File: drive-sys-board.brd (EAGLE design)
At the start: 109.2 x 48.3 mm, 28 parts

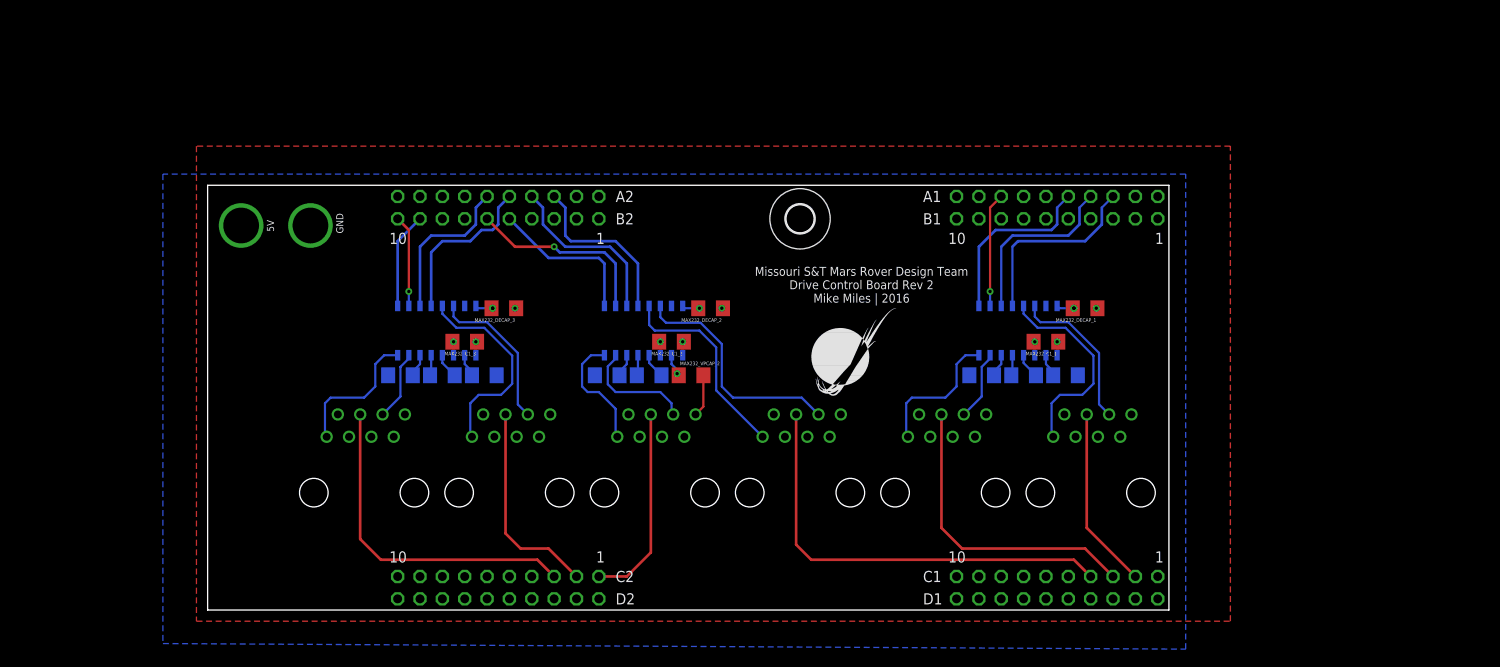
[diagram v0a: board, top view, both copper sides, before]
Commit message: Replaced RJ45 Connectors with 15-Pin D-Subs
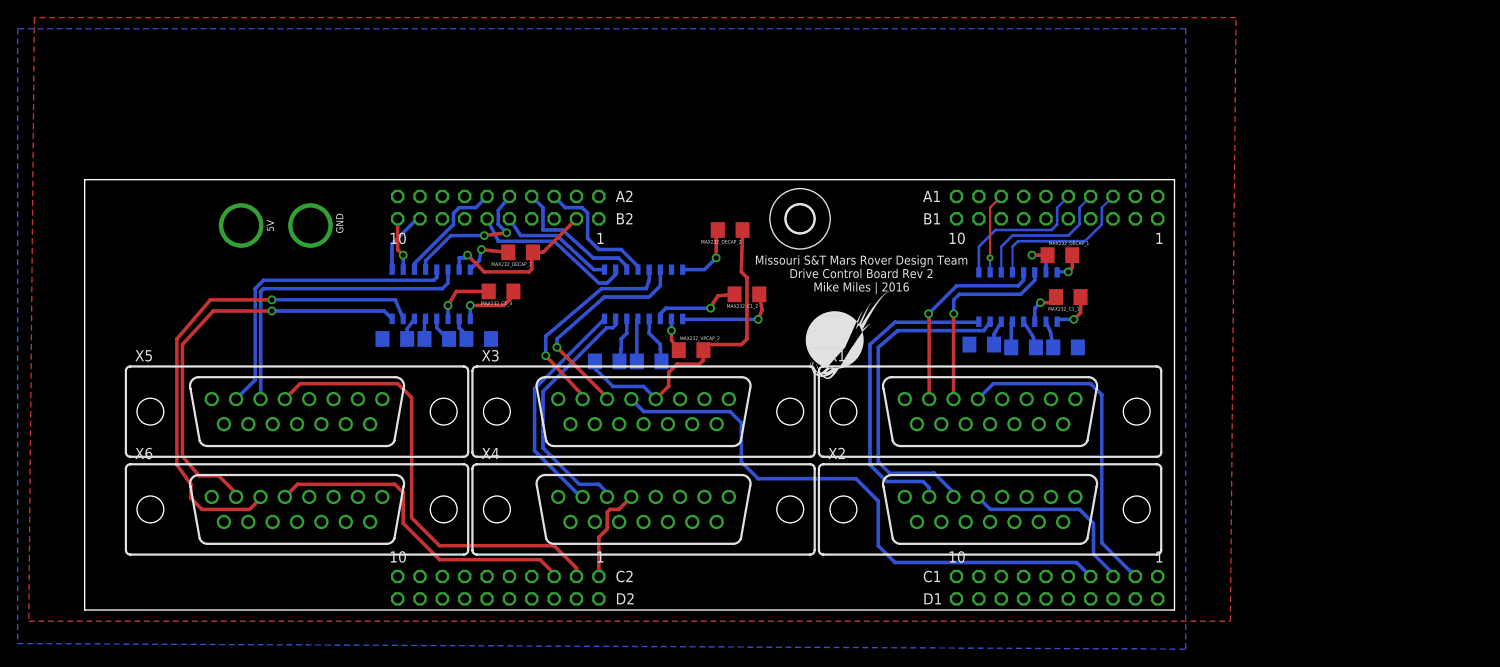
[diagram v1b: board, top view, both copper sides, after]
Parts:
- removed RJ45_1, RJ45_2, RJ45_3, RJ45_4, RJ45_5, RJ45_6: RJ45KEYSTONE-949, MRDT-2015-General:KEYSTONE-949
- added X1, X2, X3, X4, X5, X6: D-SUB15-H2M15ST, con-thomas-betts:H2M15ST
- moved MAX232_C1_2 10.1 mm to (61.3, 35.9)
- moved MAX232_DECAP_2 9.16 mm to (59.4, 43.2)
- moved MAX232_C1_3 7.05 mm to (33.3, 36.2)
- moved MAX232_DECAP_1 6.68 mm to (96.8, 40.3), turned to 0 degrees
- moved MAX232_DECAP_3 6.63 mm to (35.6, 40.6)
- moved MAX232_C1_1 5.68 mm to (97.8, 35.6)
- moved MAX232_3 4.18 mm to (25.4, 35.9)
- moved MAX232_C2_3 4.18 mm to (26.0, 30.8)
- moved MAX232_VPCAP_3 4.18 mm to (30.8, 30.8)
- moved MAX232_VNCAP_3 4.18 mm to (21.3, 30.8)
- moved MAX232_2 4.13 mm to (49.5, 35.9)
- moved MAX232_1 3.81 mm to (92.1, 35.6)
- moved MAX232_VNCAP_1 3.49 mm to (87.9, 30.2)
- moved MAX232_C2_1 3.17 mm to (92.7, 29.8)
- moved MAX232_VPCAP_1 3.17 mm to (97.5, 29.8)
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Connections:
- removed net RS232_IN_4: MAX232_2.8, RJ45_4.P$1
- new net RS232_IN__4: MAX232_2.8, X4.2
- net +5V: no longer RJ45_1.P$5, RJ45_2.P$5, RJ45_3.P$5, RJ45_4.P$5, RJ45_5.P$5, RJ45_6.P$5
- net GND: now also MAX232_2.15, MAX232_3.15, X1.13, X1.5, X2.13, X2.5, X3.13, X3.5, X4.13, X4.5, X5.13, X5.5, X6.13, X6.5; no longer RJ45_1.P$2, RJ45_1.P$3, RJ45_1.P$7, RJ45_1.P$8, RJ45_2.P$2, RJ45_2.P$3, RJ45_2.P$7, RJ45_2.P$8, RJ45_3.P$2, RJ45_3.P$3, RJ45_3.P$7, RJ45_3.P$8, RJ45_4.P$2, RJ45_4.P$3, RJ45_4.P$7, RJ45_4.P$8, RJ45_5.P$2, RJ45_5.P$3, RJ45_5.P$7, RJ45_5.P$8, RJ45_6.P$2, RJ45_6.P$3, RJ45_6.P$7, RJ45_6.P$8
- net PWM_1: now also X1.4; no longer RJ45_1.P$4
- net PWM_2: now also X2.4; no longer RJ45_2.P$4
- net PWM_3: now also X3.4; no longer RJ45_3.P$4
- net PWM_4: now also X4.4; no longer RJ45_4.P$4
- net PWM_5: now also X5.4; no longer RJ45_5.P$4
- net PWM_6: now also X6.4; no longer RJ45_6.P$4
- net RS232_IN_1: now also X1.2; no longer RJ45_1.P$1
- net RS232_IN_2: now also X2.2; no longer RJ45_2.P$1
- net RS232_IN_3: now also X3.2; no longer RJ45_3.P$1
- net RS232_IN_5: now also X5.2; no longer RJ45_5.P$1
- net RS232_IN_6: now also X6.2; no longer RJ45_6.P$1
- net RS232_OUT_1: now also X1.3; no longer RJ45_1.P$6
- net RS232_OUT_2: now also X2.3; no longer RJ45_2.P$6
- net RS232_OUT_3: now also X3.3; no longer RJ45_3.P$6
- net RS232_OUT_4: now also X4.3; no longer RJ45_4.P$6
- net RS232_OUT_5: now also X5.3; no longer RJ45_5.P$6
- net RS232_OUT_6: now also X6.3; no longer RJ45_6.P$6
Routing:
- net GND: track 4.81 -> 61.3 mm, vias 3 -> 2
- net RS232_OUT_6: track 7.96 -> 56.9 mm, vias 0 -> 1
- net RS232_IN_6: track 15.9 -> 46.9 mm, vias 0 -> 1
- net RS232_OUT_2: track 7.96 -> 37.4 mm
- net PWM_5: track 23.6 -> 51.5 mm
- net RS232_IN__4: track 0.00 -> 25.9 mm
- net RS232_IN_2: track 15.9 -> 35.9 mm
- net RS232_OUT_5: track 17.7 -> 35.4 mm
- net PWM_1: track 20.7 -> 37.6 mm
- net PWM_3: track 49.8 -> 66.1 mm
- net RS232_OUT_4: track 13.1 -> 28.4 mm
- net RS232_IN_4: track 13.6 -> 0.00 mm
- net PWM_2: track 34.7 -> 21.3 mm
- net RS232_IN_5: track 23.6 -> 35.5 mm
- net PWM_4: track 22.7 -> 11.2 mm
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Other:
- board size 109.2 x 48.3 mm -> 123.8 x 48.9 mm

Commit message: Updated connectors and UART hardware
- Replaced DSubs with Molex-SL 5-pin Connectors
- Swapped MAX3232 for MAX3078
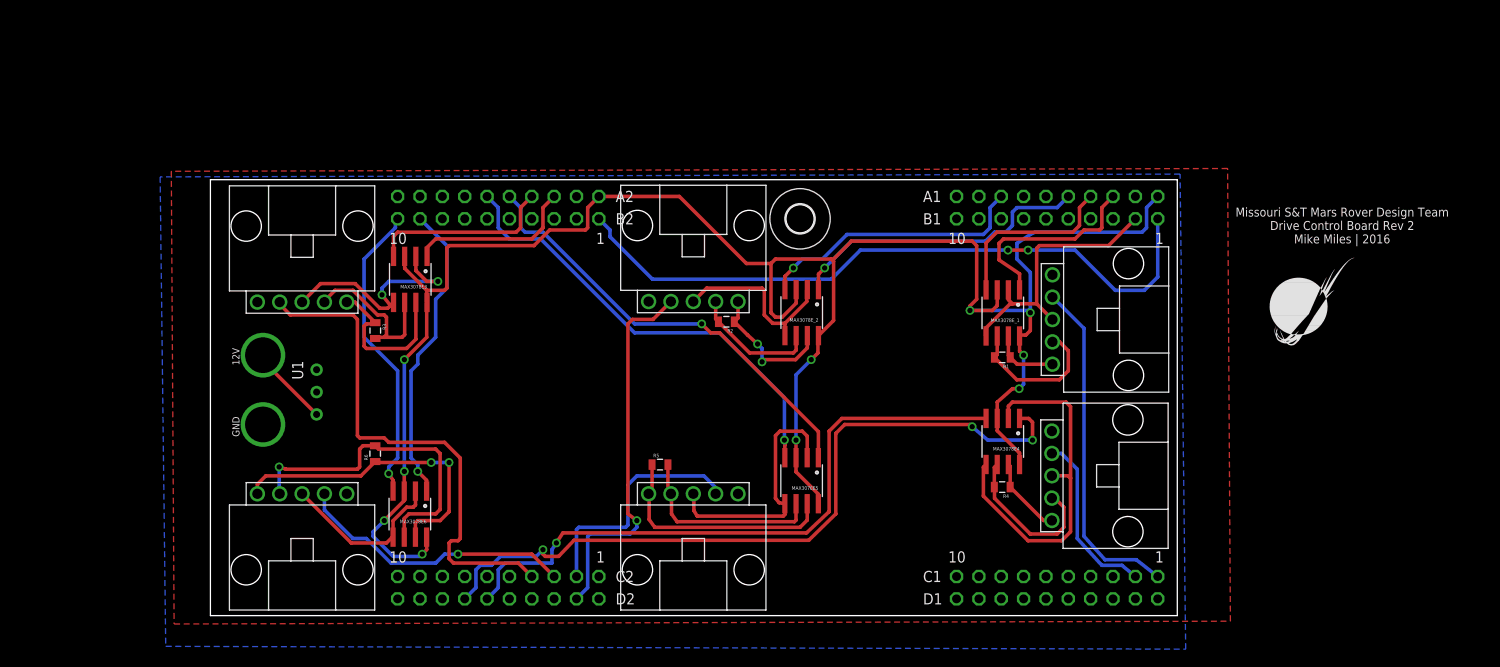
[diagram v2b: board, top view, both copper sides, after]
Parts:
- removed MAX232_1, MAX232_2, MAX232_3: MAX3232SO16, MRDT-Digital-ICs:SO16
- removed MAX232_C1_1, MAX232_C1_2: .047uF, SparkFun-Capacitors:1206
- removed MAX232_C1_3: 0.047uF, SparkFun-Capacitors:1206
- removed MAX232_C2_1, MAX232_C2_2, MAX232_C2_3, MAX232_VNCAP_1, MAX232_VNCAP_2, MAX232_VNCAP_3, MAX232_VPCAP_1, MAX232_VPCAP_2, MAX232_VPCAP_3: 0.33uF, SparkFun-Capacitors:1206
- removed MAX232_DECAP_1, MAX232_DECAP_2, MAX232_DECAP_3: 0.1uF, SparkFun-Capacitors:1206
- removed U$7: APP_2POS_CONFIG5V_VERT, MRDT-Connectors:APP45_5V_VERT_CONFIG
- removed X1, X2, X3, X4, X5, X6: D-SUB15-H2M15ST, con-thomas-betts:H2M15ST
- added CONN_1, CONN_2, CONN_3, CONN_4, CONN_5, CONN_6: 5PIN, Molex-SL:5PIN
- added J1: APP_2POS_CONFIG12V_VERT, MRDT-Connectors:APP45_12V_VERT_CONFIG
- added MAX3078E3, MAX3078E4, MAX3078E5, MAX3078E6, MAX3078E_1, MAX3078E_2: MAX3078E, MRDT-ICs:SOIC8
- added R1, R2, R3, R4, R5, R6: 120, SparkFun-Passives:0805
- added U1: OKI-78SR-5/1.5-W36HC, MRDT-ICs:OKI-78SR_HORIZ
- moved U$2 52.8 mm to (120.7, 29.2)
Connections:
- removed net N$1_1: MAX232_1.1, MAX232_C1_1.1
- removed net N$1_2: MAX232_2.1, MAX232_C1_2.1
- removed net N$1_3: MAX232_3.1, MAX232_C1_3.1
- removed net N$2_1: MAX232_1.2, MAX232_VPCAP_1.1
- removed net N$2_2: MAX232_2.2, MAX232_VPCAP_2.1
- removed net N$2_3: MAX232_3.2, MAX232_VPCAP_3.1
- removed net N$3_1: MAX232_1.3, MAX232_C1_1.2
- removed net N$3_2: MAX232_2.3, MAX232_C1_2.2
- removed net N$3_3: MAX232_3.3, MAX232_C1_3.2
- removed net N$4_1: MAX232_1.4, MAX232_C2_1.1
- removed net N$4_2: MAX232_2.4, MAX232_C2_2.1
- removed net N$4_3: MAX232_3.4, MAX232_C2_3.1
- removed net N$5_1: MAX232_1.5, MAX232_C2_1.2
- removed net N$5_2: MAX232_2.5, MAX232_C2_2.2
- removed net N$5_3: MAX232_3.5, MAX232_C2_3.2
- removed net N$6_1: MAX232_1.6, MAX232_VNCAP_1.1
- removed net N$6_2: MAX232_2.6, MAX232_VNCAP_2.1
- removed net N$6_3: MAX232_3.6, MAX232_VNCAP_3.1
- removed net RS232_IN_1: MAX232_1.13, X1.2
- removed net RS232_IN_2: MAX232_1.8, X2.2
- removed net RS232_IN_3: MAX232_2.13, X3.2
- removed net RS232_IN_5: MAX232_3.13, X5.2
- removed net RS232_IN_6: MAX232_3.8, X6.2
- removed net RS232_IN__4: MAX232_2.8, X4.2
- removed net RS232_OUT_1: MAX232_1.14, X1.3
- removed net RS232_OUT_2: MAX232_1.7, X2.3
- removed net RS232_OUT_3: MAX232_2.14, X3.3
- removed net RS232_OUT_4: MAX232_2.7, X4.3
- removed net RS232_OUT_5: MAX232_3.14, X5.3
- removed net RS232_OUT_6: MAX232_3.7, X6.3
- new net 3.3V: MAX3078E3.3, MAX3078E3.8, MAX3078E4.3, MAX3078E4.8, MAX3078E5.3, MAX3078E5.8, MAX3078E6.3, MAX3078E6.8, MAX3078E_1.3, MAX3078E_1.8, MAX3078E_2.3, MAX3078E_2.8, U$1.+3V3_1, U$1.+3V3_2
- new net N$10: CONN_3.1, MAX3078E3.7, R3.1
- new net N$12: CONN_4.2, MAX3078E4.6, R4.2
- new net N$13: CONN_4.1, MAX3078E4.7, R4.1
- new net N$15: CONN_5.2, MAX3078E5.6, R5.2
- new net N$16: CONN_5.1, MAX3078E5.7, R5.1
- new net N$18: CONN_6.2, MAX3078E6.6, R6.2
- new net N$19: CONN_6.1, MAX3078E6.7, R6.1
- new net N$3: CONN_1.2, MAX3078E_1.6, R1.2
- new net N$4: CONN_1.1, MAX3078E_1.7, R1.1
- new net N$5: J1.VCC, U1.1
- new net N$6: CONN_2.2, MAX3078E_2.6, R2.2
- new net N$7: CONN_2.1, MAX3078E_2.7, R2.1
- new net N$9: CONN_3.2, MAX3078E3.6, R3.2
- new net VCC: U$1.+5V_1, U$1.+5V_2
- net +5V: now also U1.3; no longer MAX232_1.16, MAX232_2.16, MAX232_3.16, MAX232_DECAP_1.2, MAX232_DECAP_2.2, MAX232_DECAP_3.2, U$1.+5V_1, U$1.+5V_2, U$7.5V
- net GND: now also CONN_1.3, CONN_2.3, CONN_3.3, CONN_4.3, CONN_5.3, CONN_6.3, J1.GND, MAX3078E3.2, MAX3078E3.5, MAX3078E4.2, MAX3078E4.5, MAX3078E5.2, MAX3078E5.5, MAX3078E6.2, MAX3078E6.5, MAX3078E_1.2, MAX3078E_1.5, MAX3078E_2.2, MAX3078E_2.5, U1.2; no longer MAX232_1.15, MAX232_2.15, MAX232_3.15, MAX232_DECAP_1.1, MAX232_DECAP_2.1, MAX232_DECAP_3.1, MAX232_VNCAP_1.2, MAX232_VNCAP_2.2, MAX232_VNCAP_3.2, MAX232_VPCAP_1.2, MAX232_VPCAP_2.2, MAX232_VPCAP_3.2, U$7.GND, X1.13, X1.5, X2.13, X2.5, X3.13, X3.5, X4.13, X4.5, X5.13, X5.5, X6.13, X6.5
- net PWM_1: now also CONN_1.4, U$1.PF1; no longer U$1.PF2, X1.4
- net PWM_2: now also CONN_2.4, U$1.PM7; no longer U$1.PF3, X2.4
- net PWM_3: now also CONN_3.4, U$1.PM0; no longer U$1.PG0, X3.4
- net PWM_4: now also CONN_4.4, U$1.PF2; no longer U$1.PG1, X4.4
- net PWM_5: now also CONN_5.4; no longer X5.4
- net PWM_6: now also CONN_6.4; no longer X6.4
- net RX_1: now also MAX3078E_1.1; no longer MAX232_1.12
- net RX_2: now also MAX3078E_2.1; no longer MAX232_1.9
- net RX_3: now also MAX3078E3.1; no longer MAX232_2.12
- net RX_4: now also MAX3078E4.1, U$1.PQ3/PA2; no longer MAX232_2.9, U$1.PK0
- net RX_5: now also MAX3078E5.1; no longer MAX232_3.12
- net RX_6: now also MAX3078E6.1; no longer MAX232_3.9
- net TX_1: now also MAX3078E_1.4; no longer MAX232_1.11
- net TX_2: now also MAX3078E_2.4; no longer MAX232_1.10
- net TX_3: now also MAX3078E3.4; no longer MAX232_2.11
- net TX_4: now also MAX3078E4.4, U$1.PQ2/PA3; no longer MAX232_2.10, U$1.PK1
- net TX_5: now also MAX3078E5.4; no longer MAX232_3.11
- net TX_6: now also MAX3078E6.4; no longer MAX232_3.10
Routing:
- net 3.3V: track 0.00 -> 229.8 mm, vias 0 -> 10
- net GND: track 61.3 -> 167.9 mm
- net VCC: track 0.00 -> 77.3 mm, vias 0 -> 2
- net RX_4: track 13.3 -> 84.6 mm, vias 0 -> 3
- net RS232_OUT_6: track 56.9 -> 0.00 mm, vias 1 -> 0
- net TX_4: track 19.0 -> 72.8 mm, vias 0 -> 1
- net RS232_IN_6: track 46.9 -> 0.00 mm, vias 1 -> 0
- net TX_5: track 12.9 -> 51.4 mm, vias 0 -> 1
- net RS232_OUT_2: track 37.4 -> 0.00 mm
- net N$18: track 0.00 -> 37.0 mm, vias 0 -> 1
- net RS232_IN_2: track 35.9 -> 0.00 mm
- net N$19: track 0.00 -> 35.5 mm, vias 0 -> 2
- net RS232_IN_5: track 35.5 -> 0.00 mm
- net RS232_OUT_5: track 35.4 -> 0.00 mm
- net RX_5: track 16.4 -> 50.5 mm, vias 2 -> 1
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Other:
- board size 123.8 x 48.9 mm -> 109.9 x 49.5 mm

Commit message: Flipped 5Pin Connector to avoid twisted wires
Mirrored the connector in the schematic and rerouted the necessary wires
in the board file.
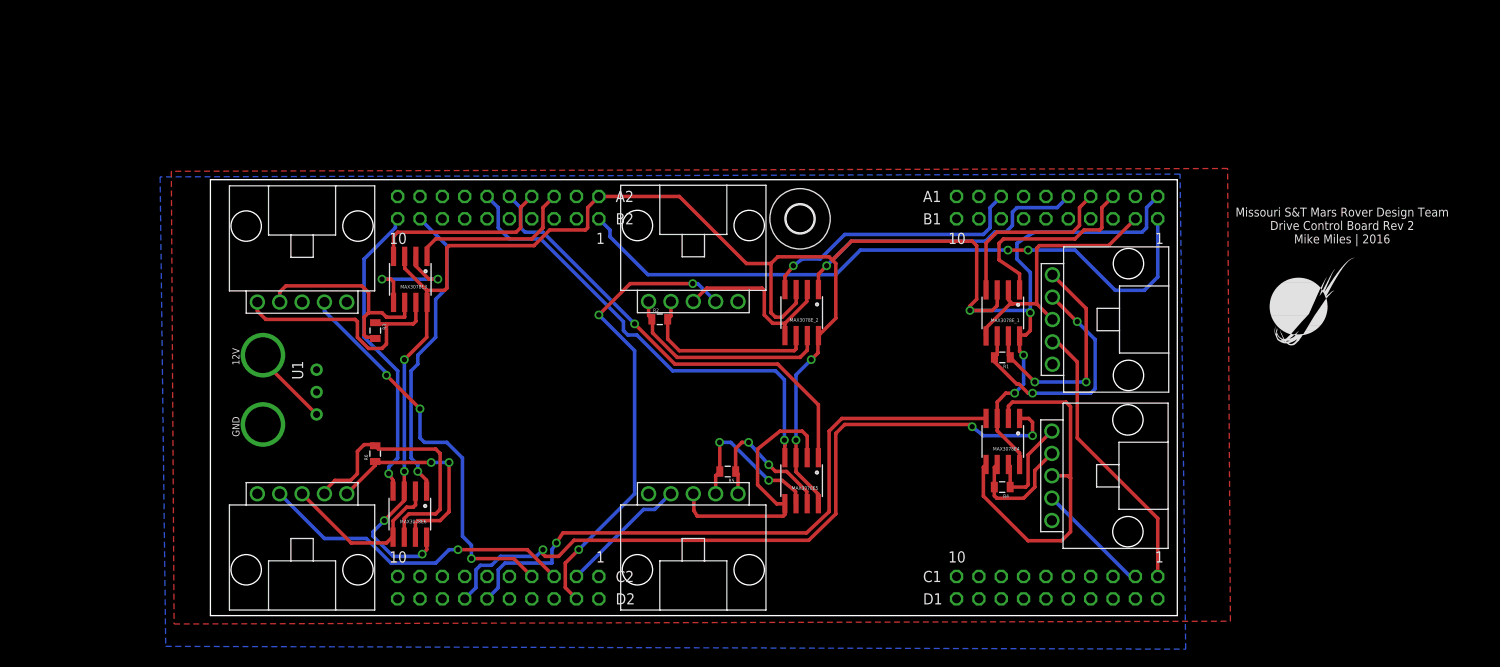
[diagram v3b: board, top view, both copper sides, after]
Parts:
- moved R5 7.74 mm to (59.1, 15.7), turned to 180 degrees
- moved R2 7.57 mm to (51.4, 33.0), turned to 0 degrees
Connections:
- net 3.3V renamed +3V3
- net N$10: now also CONN_3.5; no longer CONN_3.1
- net N$12: now also CONN_4.4; no longer CONN_4.2
- net N$13: now also CONN_4.5; no longer CONN_4.1
- net N$15: now also CONN_5.4; no longer CONN_5.2
- net N$16: now also CONN_5.5; no longer CONN_5.1
- net N$18: now also CONN_6.4; no longer CONN_6.2
- net N$19: now also CONN_6.5; no longer CONN_6.1
- net N$3: now also CONN_1.4; no longer CONN_1.2
- net N$4: now also CONN_1.5; no longer CONN_1.1
- net N$6: now also CONN_2.4; no longer CONN_2.2
- net N$7: now also CONN_2.5; no longer CONN_2.1
- net N$9: now also CONN_3.4; no longer CONN_3.2
- net PWM_1: now also CONN_1.2; no longer CONN_1.4
- net PWM_2: now also CONN_2.2; no longer CONN_2.4
- net PWM_3: now also CONN_3.2; no longer CONN_3.4
- net PWM_4: now also CONN_4.2; no longer CONN_4.4
- net PWM_5: now also CONN_5.2; no longer CONN_5.4
- net PWM_6: now also CONN_6.2; no longer CONN_6.4
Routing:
- net N$4: track 7.64 -> 26.1 mm, vias 0 -> 2
- net PWM_3: track 58.4 -> 45.3 mm, vias 0 -> 3
- net PWM_5: track 27.6 -> 14.6 mm
- net N$3: track 16.9 -> 28.6 mm, vias 0 -> 2
- net N$19: track 35.5 -> 25.0 mm
- net PWM_2: track 43.2 -> 53.3 mm, vias 1 -> 3
- net GND: track 167.9 -> 158.2 mm
- net N$10: track 18.5 -> 27.9 mm
- net N$16: track 27.0 -> 17.7 mm, vias 0 -> 2
- net N$7: track 15.6 -> 24.5 mm, vias 2 -> 0
- net PWM_1: track 38.9 -> 31.9 mm
- net PWM_4: track 19.9 -> 13.2 mm
- net N$6: track 14.5 -> 21.1 mm
- net N$18: track 37.0 -> 30.5 mm, vias 1 -> 0
- net N$9: track 18.5 -> 24.3 mm
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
